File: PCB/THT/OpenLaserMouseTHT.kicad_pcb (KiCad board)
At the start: 2 copper layers, 56 x 84 mm, 24 parts, among them J1 Amiga_Conn, M1 ADNS-9800, Q1 ZVP2106A, SW2 LEFT, SW3 RIGHT

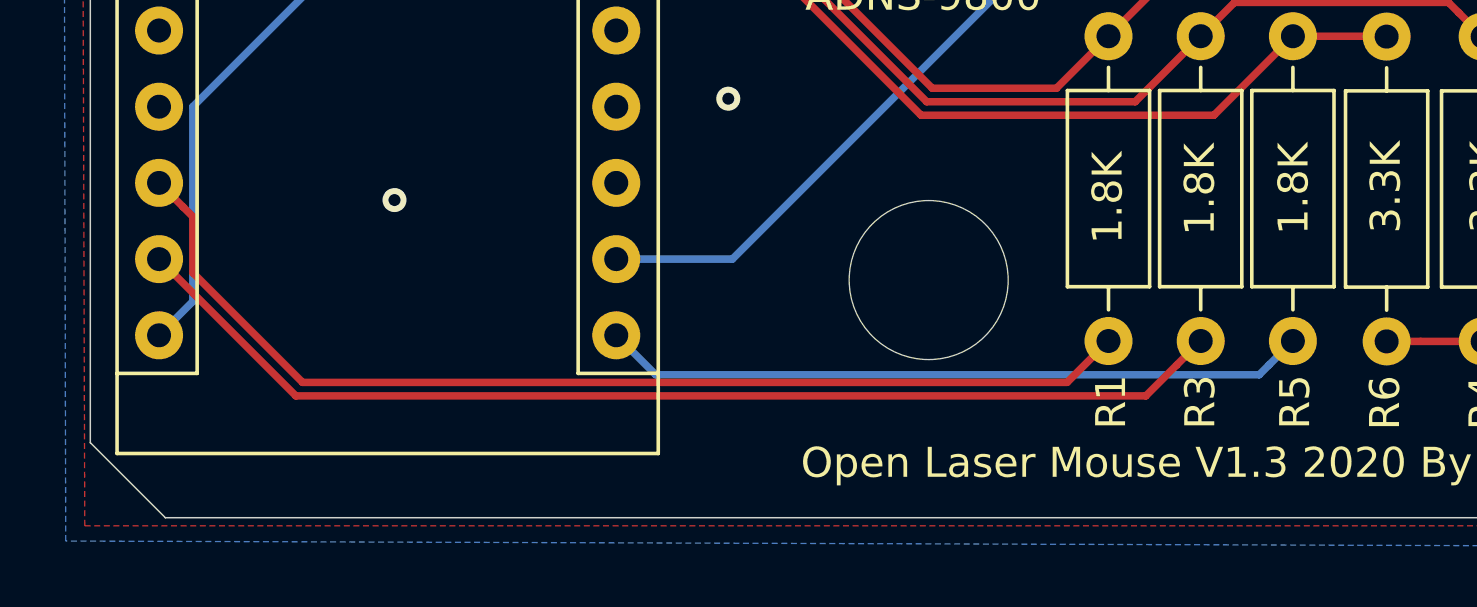
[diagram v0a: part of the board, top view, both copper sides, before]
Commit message: Adjustments and Photos
Adjusted Mouting Holes on the PCB's
Added Photos of V1.1
Tidy up
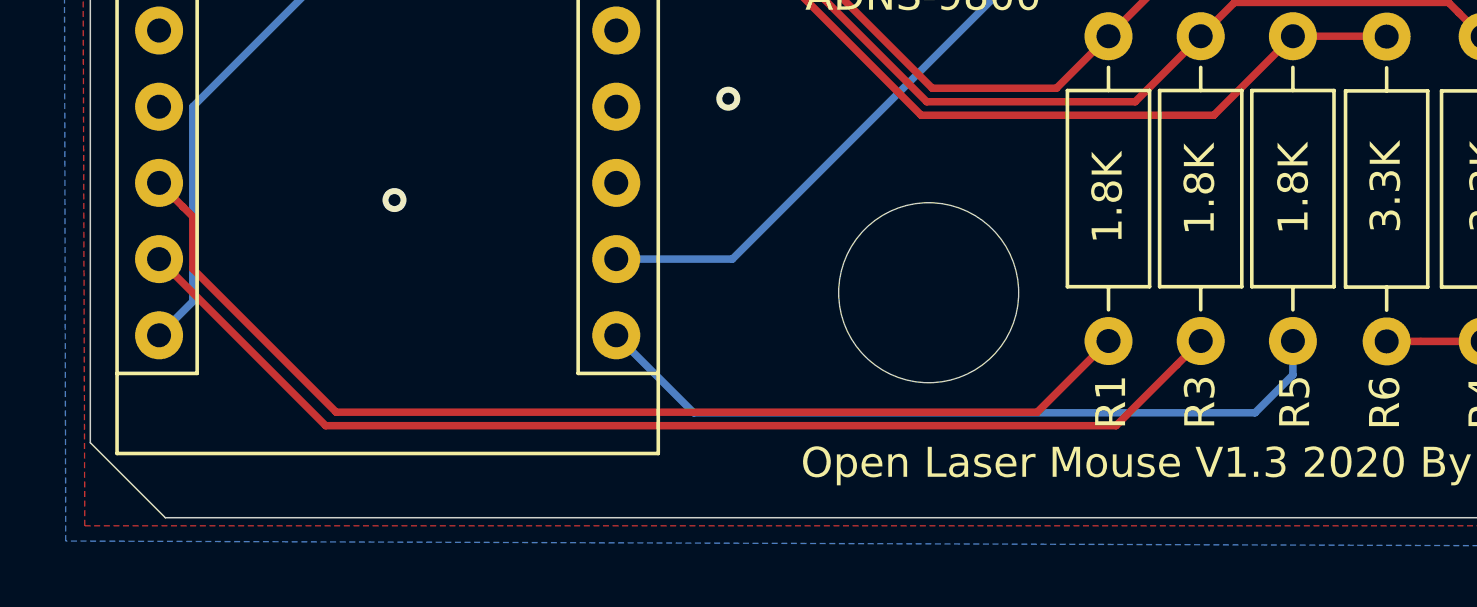
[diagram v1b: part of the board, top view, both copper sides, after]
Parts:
- moved MHe 0.42 mm to (67.9, 116.5)
- renumbered MH2 to MHe
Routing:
- net SCLK-H: track 23.6 -> 25.3 mm
- net MOSI-H: track 37.4 -> 38.2 mm
- net NCS-H: track 36.1 -> 36.8 mm
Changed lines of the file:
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@@
     (mod_text_size 1 1)
     (mod_text_width 0.15)
-    (pad_size 3 3)
-    (pad_drill 1.5)
+    (pad_size 6 6)
+    (pad_drill 6)
     (pad_to_mask_clearance 0.051)
     (solder_mask_min_width 0.25)
@@
   )
   (module MountingHole:MountingHole_5.3mm_M5 (layer F.Cu)
-    (at 67.945 116.078)
+    (at 67.945 116.5)
     (descr "Mounting Hole 5.3mm, no annular, M5")
     (tags "mounting hole 5.3mm no annular m5")
     (attr virtual)
-    (fp_text reference MH2 (at 0 -3.429) (layer F.SilkS) hide
+    (fp_text reference MHe (at 0 -3.429) (layer F.SilkS) hide
       (effects (font (size 1 1) (thickness 0.15)))
     )
@@
       (effects (font (size 1 1) (thickness 0.15)))
     )
-    (pad 1 np_thru_hole circle (at 0 0) (size 5.3 5.3) (drill 5.3) (layers *.Cu *.Mask))
+    (pad "" np_thru_hole circle (at 0 0) (size 6 6) (drill 6) (layers *.Cu *.Mask))
   )
   (module MountingHole:MountingHole_5.3mm_M5 (layer F.Cu)
@@
   (segment (start 77.487999 78.925201) (end 77.813001 78.600199) (width 0.25) (layer B.Cu) (net 14))
   (segment (start 57.531 84.8995) (end 62.224701 80.205799) (width 0.25) (layer B.Cu) (net 14))
-  (segment (start 79.286201 118.909999) (end 80.0862 118.11) (width 0.25) (layer B.Cu) (net 15))
-  (segment (start 78.961199 119.235001) (end 79.286201 118.909999) (width 0.25) (layer B.Cu) (net 15))
-  (segment (start 58.846501 119.235001) (end 78.961199 119.235001) (width 0.25) (layer B.Cu) (net 15))
-  (segment (start 57.531 117.9195) (end 58.846501 119.235001) (width 0.25) (layer B.Cu) (net 15))
+  (segment (start 80.0862 119.24137) (end 78.82489 120.50268) (width 0.25) (layer B.Cu) (net 15))
+  (segment (start 80.0862 118.11) (end 80.0862 119.24137) (width 0.25) (layer B.Cu) (net 15))
+  (segment (start 60.11418 120.50268) (end 57.531 117.9195) (width 0.25) (layer B.Cu) (net 15))
+  (segment (start 78.82489 120.50268) (end 60.11418 120.50268) (width 0.25) (layer B.Cu) (net 15))
   (segment (start 76.212801 118.909999) (end 77.0128 118.11) (width 0.25) (layer F.Cu) (net 16))
-  (segment (start 75.184 119.9388) (end 76.212801 118.909999) (width 0.25) (layer F.Cu) (net 16))
-  (segment (start 46.8503 119.9388) (end 75.184 119.9388) (width 0.25) (layer F.Cu) (net 16))
-  (segment (start 42.291 115.3795) (end 46.8503 119.9388) (width 0.25) (layer F.Cu) (net 16))
-  (segment (start 73.9394 118.11) (end 72.56061 119.48879) (width 0.25) (layer F.Cu) (net 17))
-  (segment (start 72.56061 119.48879) (end 47.07339 119.48879) (width 0.25) (layer F.Cu) (net 17))
+  (segment (start 47.84387 120.93237) (end 74.19043 120.93237) (width 0.25) (layer F.Cu) (net 16))
+  (segment (start 74.19043 120.93237) (end 76.212801 118.909999) (width 0.25) (layer F.Cu) (net 16))
+  (segment (start 42.291 115.3795) (end 47.84387 120.93237) (width 0.25) (layer F.Cu) (net 16))
+  (segment (start 43.090999 113.639499) (end 42.291 112.8395) (width 0.25) (layer F.Cu) (net 17))
   (segment (start 43.416001 113.964501) (end 43.090999 113.639499) (width 0.25) (layer F.Cu) (net 17))
-  (segment (start 43.416001 115.831401) (end 43.416001 113.964501) (width 0.25) (layer F.Cu) (net 17))
-  (segment (start 43.090999 113.639499) (end 42.291 112.8395) (width 0.25) (layer F.Cu) (net 17))
-  (segment (start 47.07339 119.48879) (end 43.416001 115.831401) (width 0.25) (layer F.Cu) (net 17))
+  (segment (start 73.9394 118.11) (end 71.56704 120.48236) (width 0.25) (layer F.Cu) (net 17))
+  (segment (start 71.56704 120.48236) (end 48.19396 120.48236) (width 0.25) (layer F.Cu) (net 17))
+  (segment (start 43.416001 115.704401) (end 43.416001 113.964501) (width 0.25) (layer F.Cu) (net 17))
+  (segment (start 48.19396 120.48236) (end 43.416001 115.704401) (width 0.25) (layer F.Cu) (net 17))
   (segment (start 74.322 102.46) (end 61.4025 115.3795) (width 0.25) (layer B.Cu) (net 18) (status 10))
   (segment (start 61.4025 115.3795) (end 57.531 115.3795) (width 0.25) (layer B.Cu) (net 18) (status 20))
